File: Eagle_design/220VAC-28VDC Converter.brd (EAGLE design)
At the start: 160 x 100 mm, 6 parts, among them J1 1X2-3.5MM, J2 1X2-3.5MM

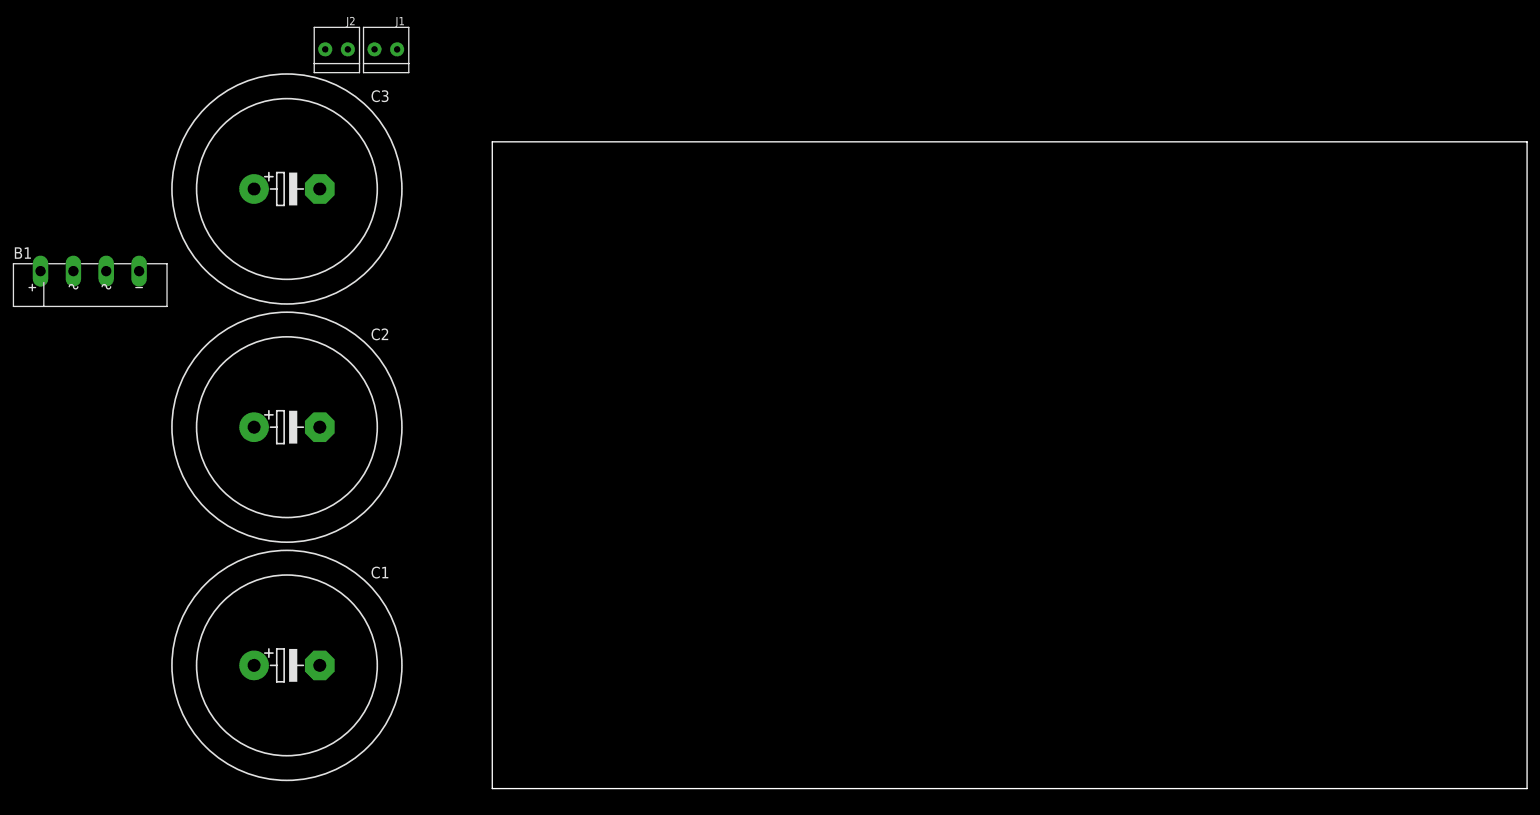
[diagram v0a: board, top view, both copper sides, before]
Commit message: Adds the brd file. This design uses 3 10mF caps in parallel
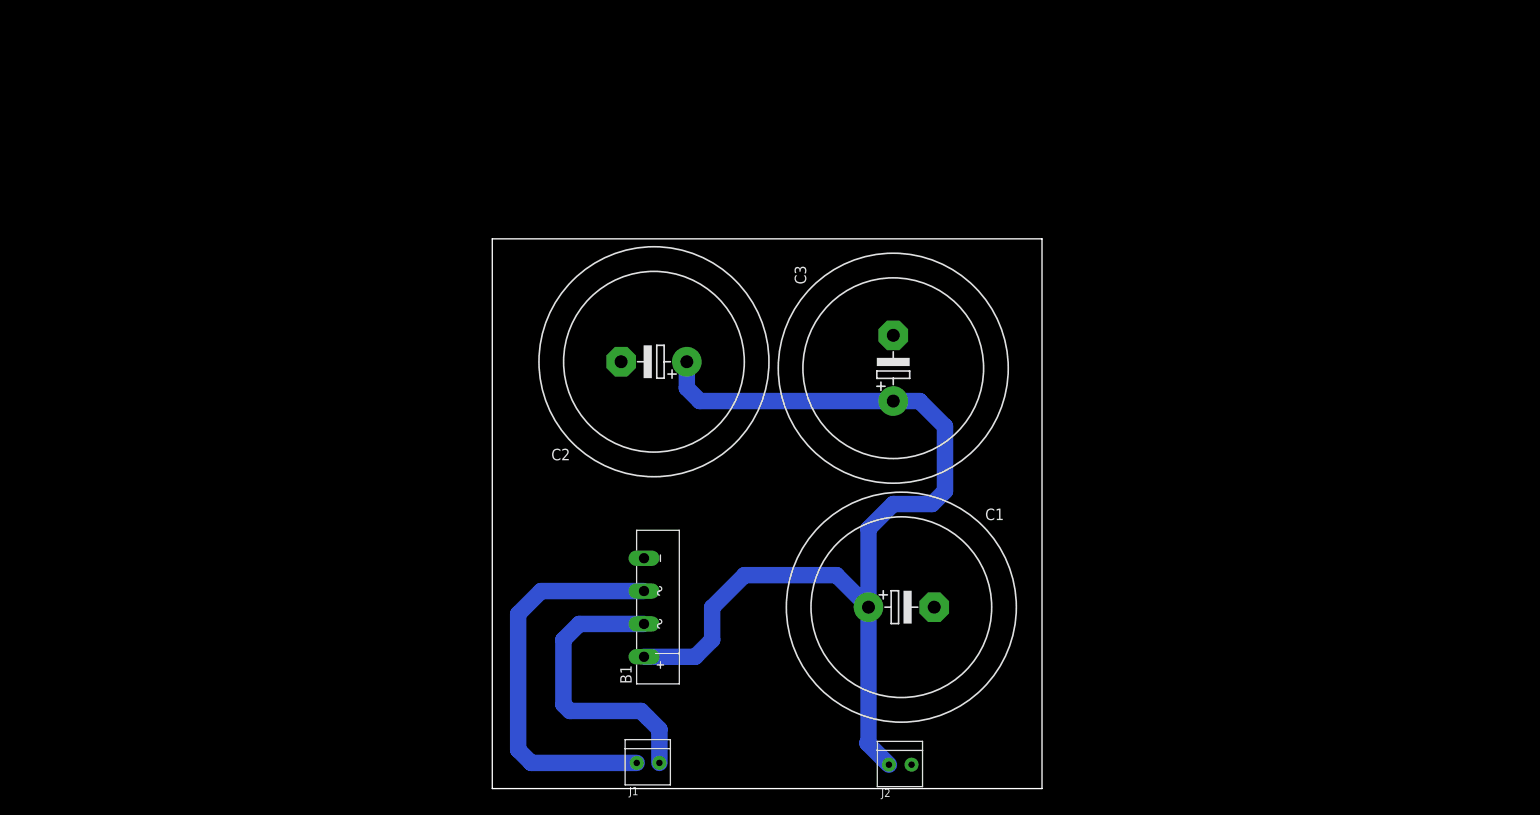
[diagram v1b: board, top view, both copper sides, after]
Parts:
- moved J2 140.9 mm to (63.1, 3.70), turned to 180 degrees
- moved J1 117.6 mm to (24.1, 3.97), turned to 180 degrees
- moved B1 101.2 mm to (26.0, 28.0), turned to 90 degrees
- moved C3 97.8 mm to (62.0, 65.0), turned to 90 degrees
- moved C1 95.4 mm to (63.2, 28.1)
- moved C2 57.6 mm to (25.0, 66.0), turned to 180 degrees
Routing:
- net N$4: track 0.00 -> 153.5 mm
- net N$2: track 0.00 -> 61.1 mm
- net N$1: track 0.00 -> 45.1 mm
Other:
- board size 160 x 100 mm -> 85 x 85 mm
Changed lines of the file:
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@@
 <setting verticaltext="up"/>
 </settings>
-<grid distance="50" unitdist="mil" unit="mil" style="lines" multiple="1" display="no" altdistance="5" altunitdist="mil" altunit="mil"/>
+<grid distance="1" unitdist="mm" unit="mm" style="lines" multiple="1" display="yes" altdistance="1" altunitdist="mm" altunit="mm"/>
 <layers>
 <layer number="1" name="Top" color="4" fill="1" visible="yes" active="yes"/>
@@
 <board>
 <plain>
-<wire x1="0" y1="0" x2="160" y2="0" width="0" layer="20"/>
-<wire x1="160" y1="0" x2="160" y2="100" width="0" layer="20"/>
-<wire x1="160" y1="100" x2="0" y2="100" width="0" layer="20"/>
-<wire x1="0" y1="100" x2="0" y2="0" width="0" layer="20"/>
+<wire x1="0" y1="0" x2="85" y2="0" width="0" layer="20"/>
+<wire x1="85" y1="0" x2="85" y2="85" width="0" layer="20"/>
+<wire x1="85" y1="85" x2="0" y2="85" width="0" layer="20"/>
+<wire x1="0" y1="85" x2="0" y2="0" width="0" layer="20"/>
+<dimension x1="0" y1="0" x2="85" y2="0" x3="42.5" y3="-10" textsize="1.778" layer="20"/>
+<dimension x1="85" y1="0" x2="85" y2="90" x3="97" y3="45" textsize="1.778" layer="20"/>
 </plain>
 <attributes>
@@
 </class>
 </classes>
-<designrules name="default">
+<designrules name="default *">
 <description language="de">&lt;b&gt;EAGLE Design Rules&lt;/b&gt;
 &lt;p&gt;
@@
 <param name="mtCopper" value="0.035mm 0.035mm 0.035mm 0.035mm 0.035mm 0.035mm 0.035mm 0.035mm 0.035mm 0.035mm 0.035mm 0.035mm 0.035mm 0.035mm 0.035mm 0.035mm"/>
 <param name="mtIsolate" value="1.5mm 0.15mm 0.2mm 0.15mm 0.2mm 0.15mm 0.2mm 0.15mm 0.2mm 0.15mm 0.2mm 0.15mm 0.2mm 0.15mm 0.2mm"/>
-<param name="mdWireWire" value="6mil"/>
-<param name="mdWirePad" value="6mil"/>
-<param name="mdWireVia" value="6mil"/>
+<param name="mdWireWire" value="0.5mm"/>
+<param name="mdWirePad" value="1mm"/>
+<param name="mdWireVia" value="2.5mm"/>
 <param name="mdPadPad" value="6mil"/>
-<param name="mdPadVia" value="6mil"/>
-<param name="mdViaVia" value="6mil"/>
+<param name="mdPadVia" value="1mm"/>
+<param name="mdViaVia" value="2.5mm"/>
 <param name="mdSmdPad" value="6mil"/>
 <param name="mdSmdVia" value="6mil"/>
@@
 </autorouter>
 <elements>
-<element name="B1" library="rectifier" library_urn="urn:adsk.eagle:library:336" package="KBU" package3d_urn="urn:adsk.eagle:package:23885/1" value="" x="-62.23" y="77.47"/>
-<element name="C1" library="rcl" library_urn="urn:adsk.eagle:library:334" package="EB35D" package3d_urn="urn:adsk.eagle:package:23395/1" value="10mF" x="-31.75" y="19.05">
-<attribute name="SPICEPREFIX" value="C" x="-31.75" y="19.05" size="1.778" layer="27" display="off"/>
+<element name="B1" library="rectifier" library_urn="urn:adsk.eagle:library:336" package="KBU" package3d_urn="urn:adsk.eagle:package:23885/1" value="" x="26" y="28" rot="R90"/>
+<element name="C1" library="rcl" library_urn="urn:adsk.eagle:library:334" package="EB35D" package3d_urn="urn:adsk.eagle:package:23395/1" value="10mF" x="63.25" y="28.05">
+<attribute name="SPICEPREFIX" value="C" x="63.25" y="28.05" size="1.778" layer="27" display="off"/>
 </element>
-<element name="C2" library="rcl" library_urn="urn:adsk.eagle:library:334" package="EB35D" package3d_urn="urn:adsk.eagle:package:23395/1" value="10mF" x="-31.75" y="55.88">
-<attribute name="SPICEPREFIX" value="C" x="-31.75" y="55.88" size="1.778" layer="27" display="off"/>
+<element name="C2" library="rcl" library_urn="urn:adsk.eagle:library:334" package="EB35D" package3d_urn="urn:adsk.eagle:package:23395/1" value="10mF" x="25" y="66" rot="R180">
+<attribute name="SPICEPREFIX" value="C" x="25" y="66" size="1.778" layer="27" rot="R180" display="off"/>
 </element>
-<element name="C3" library="rcl" library_urn="urn:adsk.eagle:library:334" package="EB35D" package3d_urn="urn:adsk.eagle:package:23395/1" value="10mF" x="-31.75" y="92.71">
-<attribute name="SPICEPREFIX" value="C" x="-31.75" y="92.71" size="1.778" layer="27" display="off"/>
+<element name="C3" library="rcl" library_urn="urn:adsk.eagle:library:334" package="EB35D" package3d_urn="urn:adsk.eagle:package:23395/1" value="10mF" x="62" y="65" rot="R90">
+<attribute name="SPICEPREFIX" value="C" x="62" y="65" size="1.778" layer="27" rot="R90" display="off"/>
 </element>
-<element name="J1" library="adafruit" package="1X2-3.5MM" value="1X2-3.5MM" x="-16.51" y="114.3"/>
-<element name="J2" library="adafruit" package="1X2-3.5MM" value="1X2-3.5MM" x="-24.13" y="114.3"/>
+<element name="J1" library="adafruit" package="1X2-3.5MM" value="1X2-3.5MM" x="24.14" y="3.97" rot="R180"/>
+<element name="J2" library="adafruit" package="1X2-3.5MM" value="1X2-3.5MM" x="63.13" y="3.7" rot="R180"/>
 </elements>
 <signals>
@@
 <contactref element="J1" pad="2"/>
 <contactref element="B1" pad="AC1"/>
-<wire x1="-64.77" y1="80.01" x2="-18.21" y2="114.3" width="0" layer="19" extent="1-1"/>
+<wire x1="23.46" y1="25.46" x2="13.46" y2="25.46" width="2.54" layer="16"/>
+<wire x1="13.46" y1="25.46" x2="11" y2="23" width="2.54" layer="16"/>
+<wire x1="11" y1="23" x2="11" y2="13" width="2.54" layer="16"/>
+<wire x1="11" y1="13" x2="12" y2="12" width="2.54" layer="16"/>
+<wire x1="12" y1="12" x2="23" y2="12" width="2.54" layer="16"/>
+<wire x1="23" y1="12" x2="24" y2="11" width="2.54" layer="16"/>
+<wire x1="25.84" y1="3.97" x2="25.84" y2="9.16" width="2.54" layer="16"/>
+<wire x1="25.84" y1="9.16" x2="24" y2="11" width="2.54" layer="16"/>
 </signal>
 <signal name="N$2">
 <contactref element="J1" pad="1"/>
 <contactref element="B1" pad="AC2"/>
-<wire x1="-59.69" y1="80.01" x2="-14.71" y2="114.3" width="0" layer="19" extent="1-1"/>
+<wire x1="22.34" y1="3.97" x2="6.03" y2="3.97" width="2.54" layer="16"/>
+<wire x1="6.03" y1="3.97" x2="4" y2="6" width="2.54" layer="16"/>
+<wire x1="4" y1="6" x2="4" y2="27" width="2.54" layer="16"/>
+<wire x1="7.54" y1="30.54" x2="23.46" y2="30.54" width="2.54" layer="16"/>
+<wire x1="4" y1="27" x2="7.54" y2="30.54" width="2.54" layer="16"/>
 </signal>
 <signal name="GND">
@@
 <contactref element="C2" pad="-"/>
 <contactref element="C1" pad="-"/>
-<wire x1="-26.67" y1="92.71" x2="-25.83" y2="114.3" width="0" layer="19" extent="1-1"/>
-<wire x1="-54.61" y1="80.01" x2="-26.67" y2="92.71" width="0" layer="19" extent="1-1"/>
-<wire x1="-26.67" y1="55.88" x2="-26.67" y2="92.71" width="0" layer="19" extent="1-1"/>
-<wire x1="-26.67" y1="19.05" x2="-26.67" y2="55.88" width="0" layer="19" extent="1-1"/>
+<wire x1="19.92" y1="66" x2="62" y2="70.08" width="0" layer="19" extent="1-1"/>
+<wire x1="23.46" y1="35.62" x2="19.92" y2="66" width="0" layer="19" extent="1-1"/>
+<wire x1="68.33" y1="28.05" x2="62" y2="70.08" width="0" layer="19" extent="1-1"/>
+<wire x1="64.83" y1="3.7" x2="68.33" y2="28.05" width="0" layer="19" extent="1-1"/>
 </signal>
 <signal name="N$4">
@@
 <contactref element="C2" pad="+"/>
 <contactref element="C3" pad="+"/>
-<wire x1="-36.83" y1="92.71" x2="-22.33" y2="114.3" width="0" layer="19" extent="1-1"/>
-<wire x1="-69.85" y1="80.01" x2="-36.83" y2="92.71" width="0" layer="19" extent="1-1"/>
-<wire x1="-36.83" y1="55.88" x2="-36.83" y2="92.71" width="0" layer="19" extent="1-1"/>
-<wire x1="-36.83" y1="19.05" x2="-36.83" y2="55.88" width="0" layer="19" extent="1-1"/>
+<wire x1="23.46" y1="20.38" x2="31.38" y2="20.38" width="2.54" layer="16"/>
+<wire x1="31.38" y1="20.38" x2="34" y2="23" width="2.54" layer="16"/>
+<wire x1="34" y1="23" x2="34" y2="28" width="2.54" layer="16"/>
+<wire x1="61.33" y1="3.7" x2="58" y2="7.03" width="2.54" layer="16"/>
+<wire x1="39" y1="33" x2="34" y2="28" width="2.54" layer="16"/>
+<wire x1="58.17" y1="28.05" x2="53.22" y2="33" width="2.54" layer="16"/>
+<wire x1="53.22" y1="33" x2="39" y2="33" width="2.54" layer="16"/>
+<wire x1="58" y1="7.03" x2="58.17" y2="7.2" width="2.54" layer="16"/>
+<wire x1="58.17" y1="7.2" x2="58.17" y2="28.05" width="2.54" layer="16"/>
+<wire x1="58.17" y1="28.05" x2="58.17" y2="40.17" width="2.54" layer="16"/>
+<wire x1="58.17" y1="40.17" x2="62" y2="44" width="2.54" layer="16"/>
+<wire x1="62" y1="44" x2="68" y2="44" width="2.54" layer="16"/>
+<wire x1="70" y1="46" x2="70" y2="56" width="2.54" layer="16"/>
+<wire x1="70" y1="56" x2="66.08" y2="59.92" width="2.54" layer="16"/>
+<wire x1="66.08" y1="59.92" x2="62" y2="59.92" width="2.54" layer="16"/>
+<wire x1="68" y1="44" x2="70" y2="46" width="2.54" layer="16"/>
+<wire x1="62" y1="59.92" x2="32.08" y2="59.92" width="2.54" layer="16"/>
+<wire x1="30.08" y1="61.92" x2="30.08" y2="66" width="2.54" layer="16"/>
+<wire x1="32.08" y1="59.92" x2="30.08" y2="61.92" width="2.54" layer="16"/>
 </signal>
 </signals>

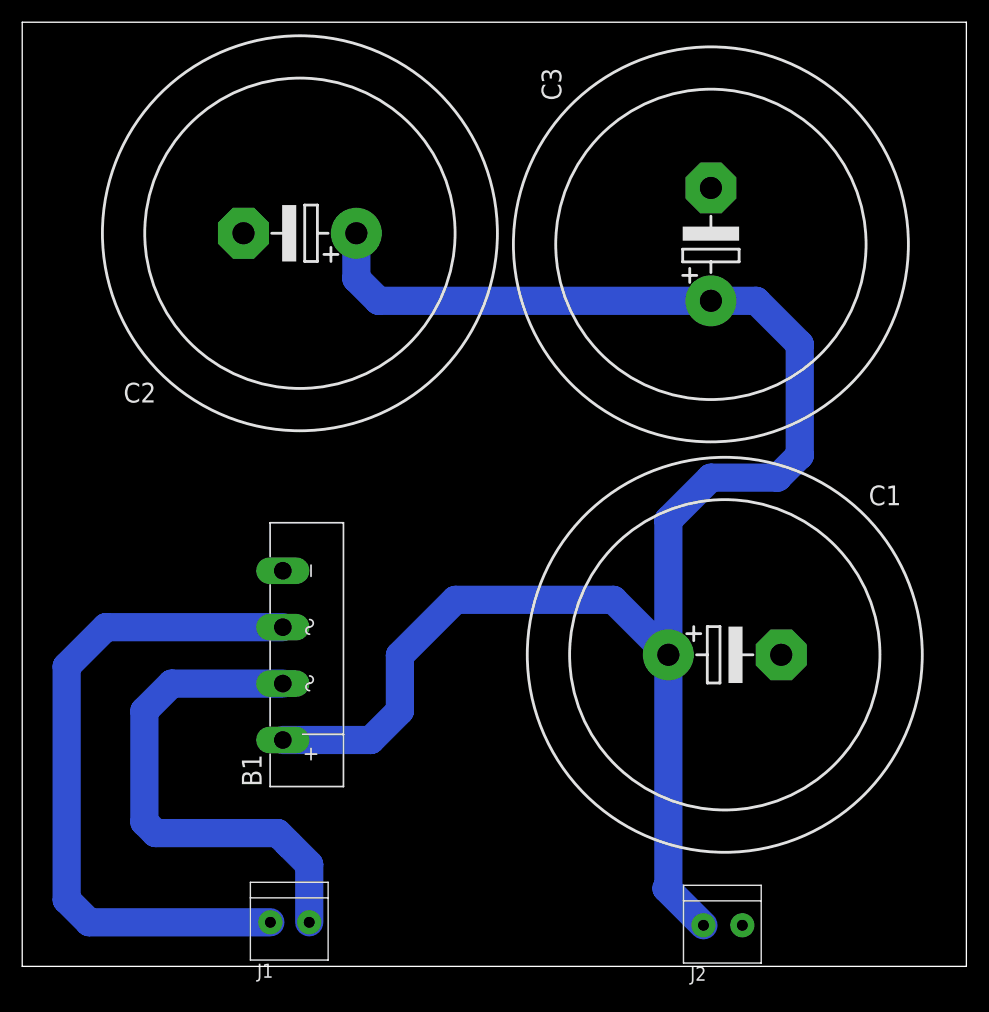
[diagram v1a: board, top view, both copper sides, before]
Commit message: Adds labels to the wire connections
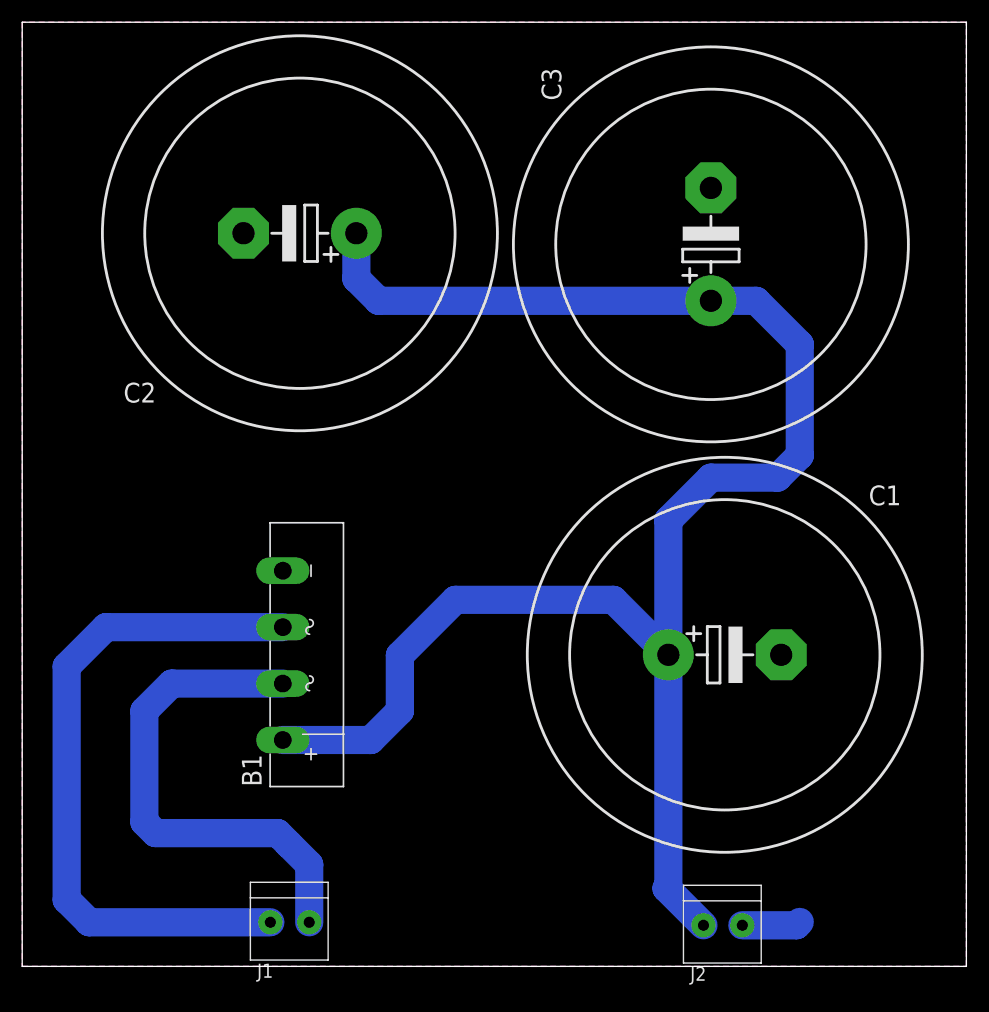
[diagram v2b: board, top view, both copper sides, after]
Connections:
- net N$1 renamed AC+VE
- net N$2 renamed AC-VE
- net N$4 renamed DC+VE
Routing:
- net GND: track 0.00 -> 5.29 mm
- added copper zone on layer 1, net GND
- added copper zone on layer 16, net GND
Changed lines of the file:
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@@
 <wire x1="0" y1="85" x2="0" y2="0" width="0" layer="20"/>
 <dimension x1="0" y1="0" x2="85" y2="0" x3="42.5" y3="-10" textsize="1.778" layer="20"/>
-<dimension x1="85" y1="0" x2="85" y2="90" x3="97" y3="45" textsize="1.778" layer="20"/>
+<dimension x1="85" y1="0" x2="85" y2="85" x3="98" y3="42.5" textsize="1.778" layer="20"/>
 </plain>
 <attributes>
@@
 </elements>
 <signals>
-<signal name="N$1">
+<signal name="AC+VE">
 <contactref element="J1" pad="2"/>
 <contactref element="B1" pad="AC1"/>
@@
 <wire x1="25.84" y1="9.16" x2="24" y2="11" width="2.54" layer="16"/>
 </signal>
-<signal name="N$2">
+<signal name="AC-VE">
 <contactref element="J1" pad="1"/>
 <contactref element="B1" pad="AC2"/>
@@
 <contactref element="C2" pad="-"/>
 <contactref element="C1" pad="-"/>
-<wire x1="19.92" y1="66" x2="62" y2="70.08" width="0" layer="19" extent="1-1"/>
-<wire x1="23.46" y1="35.62" x2="19.92" y2="66" width="0" layer="19" extent="1-1"/>
-<wire x1="68.33" y1="28.05" x2="62" y2="70.08" width="0" layer="19" extent="1-1"/>
-<wire x1="64.83" y1="3.7" x2="68.33" y2="28.05" width="0" layer="19" extent="1-1"/>
+<polygon width="2.54" layer="16" isolate="2.54">
+<vertex x="0" y="0"/>
+<vertex x="85" y="0"/>
+<vertex x="85" y="85"/>
+<vertex x="0" y="85"/>
+</polygon>
+<wire x1="64.83" y1="3.7" x2="69.7" y2="3.7" width="2.54" layer="16"/>
+<wire x1="69.7" y1="3.7" x2="70" y2="4" width="2.54" layer="16"/>
+<polygon width="2.54" layer="1">
+<vertex x="0" y="0"/>
+<vertex x="85" y="0"/>
+<vertex x="85" y="85"/>
+<vertex x="0" y="85"/>
+</polygon>
 </signal>
-<signal name="N$4">
+<signal name="DC+VE">
 <contactref element="J2" pad="1"/>
 <contactref element="B1" pad="+"/>
